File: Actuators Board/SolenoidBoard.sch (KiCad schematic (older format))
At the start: 33 parts, among them J10 Conn_01x02_Male, J9 Conn_01x02_Male, Q1 MMDT2222A

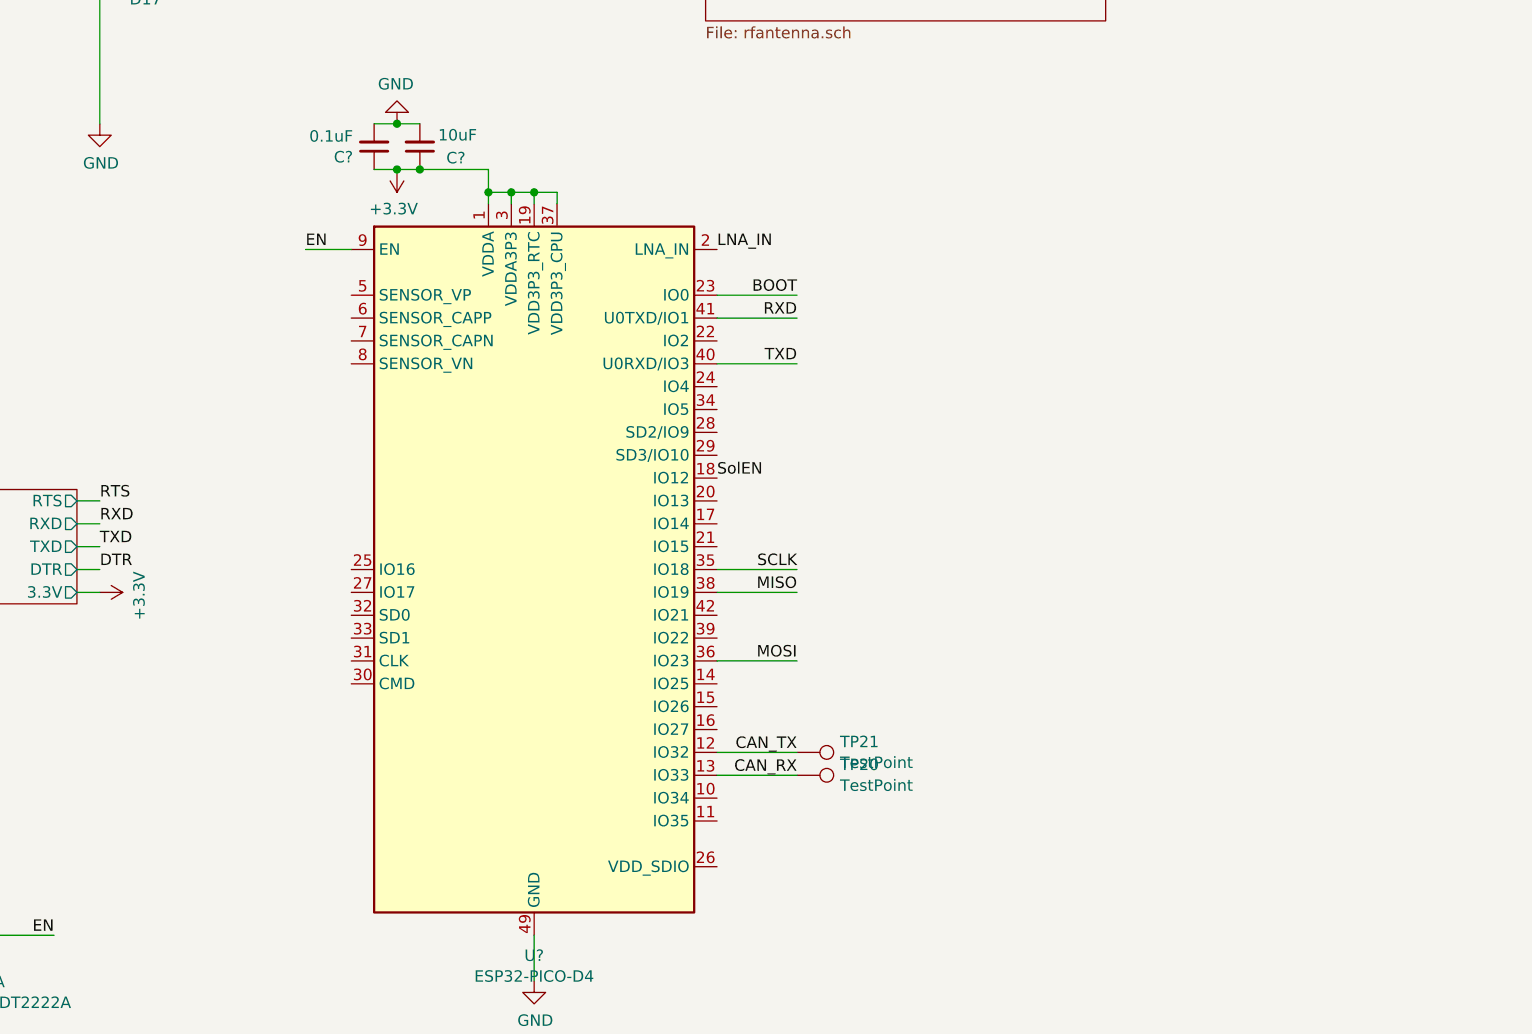
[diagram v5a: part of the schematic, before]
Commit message: added test points and power connectors (solenoid)
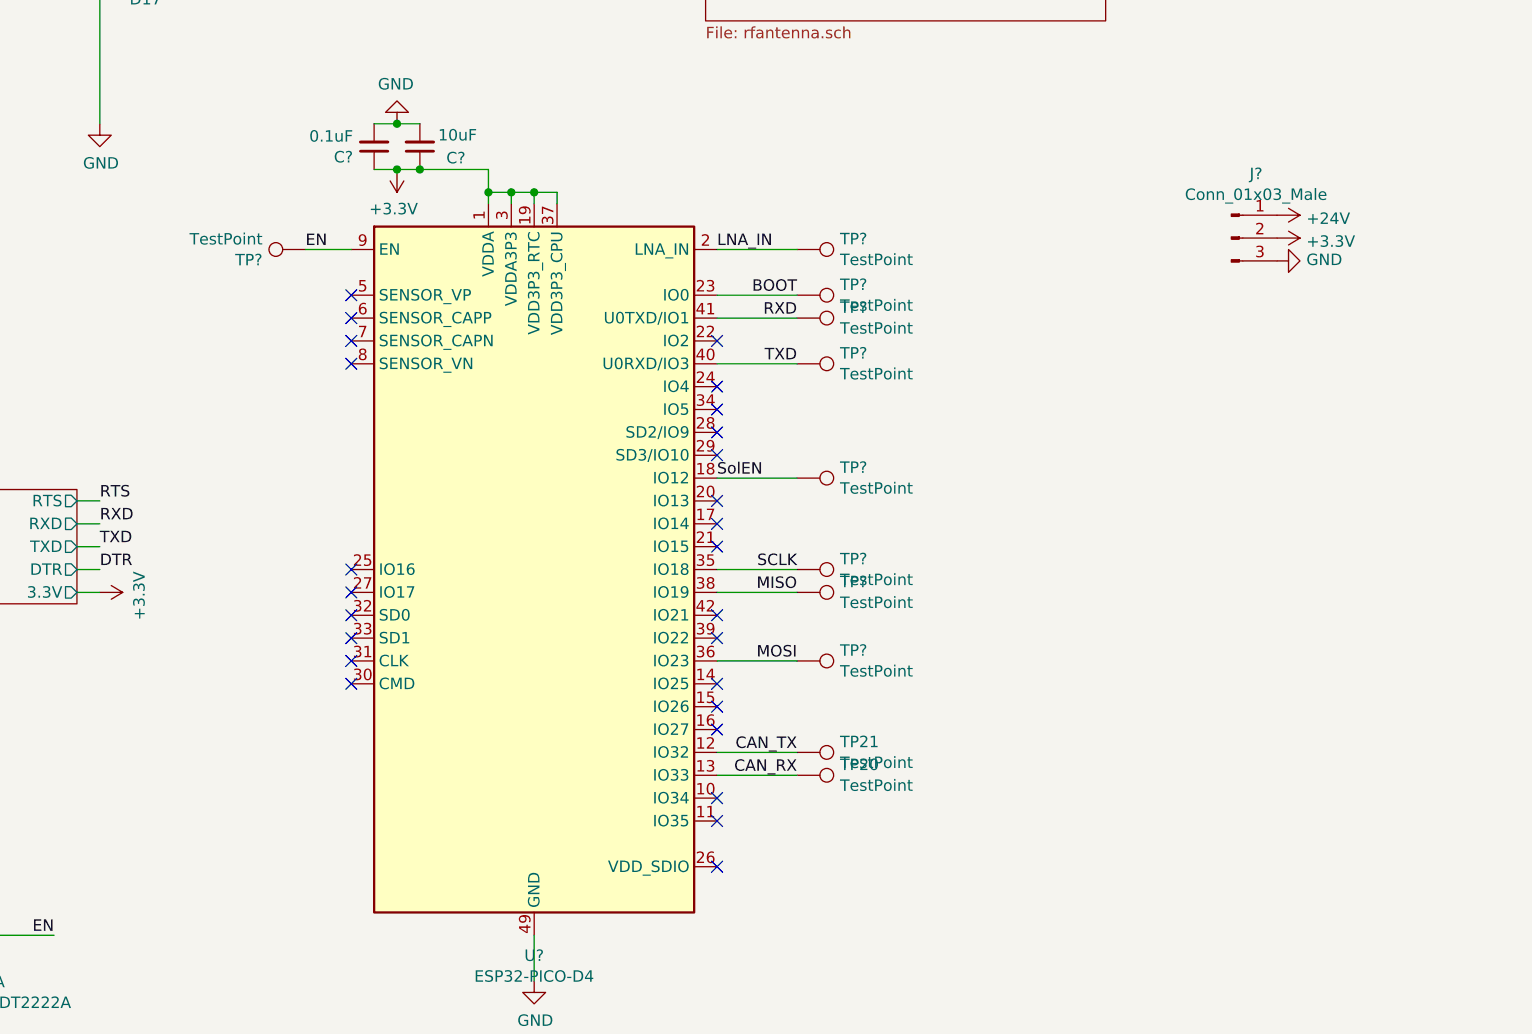
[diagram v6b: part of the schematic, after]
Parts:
- added J?: Conn_01x03_Male, symbol Connector:Conn_01x03_Male
- added TP? (x9): TestPoint, symbol Connector:TestPoint
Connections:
- net +24V: now also J?.1 (Pin_1)
- net +3V3: now also J?.2 (Pin_2)
- net BOOT: now also TP?.1
- net EN: now also TP?.1
- net GND: now also J?.3 (Pin_3)
- net LNA_IN: now also TP?.1
- net MISO: now also TP?.1
- net MOSI: now also TP?.1
- net RXD: now also TP?.1
- net SCLK: now also TP?.1
- net SolEN: now also TP?.1
- net TXD: now also TP?.1
- no-connect marks 0 -> 26
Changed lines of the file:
@@
 $EndComp
 Connection ~ 9800 2650
+$Comp
+L Connector:TestPoint TP?
+U 1 1 61AFDF58
+P 5350 2350
+F 0 "TP?" V 5304 2538 50  0000 L CNN
+F 1 "TestPoint" V 5395 2538 50  0000 L CNN
+F 2 "" H 5550 2350 50  0001 C CNN
+F 3 "~" H 5550 2350 50  0001 C CNN
+	1    5350 2350
+	0    1    1    0
+$EndComp
+$Comp
+L Connector:TestPoint TP?
+U 1 1 61AFF428
+P 5350 2450
+F 0 "TP?" V 5304 2638 50  0000 L CNN
+F 1 "TestPoint" V 5395 2638 50  0000 L CNN
+F 2 "" H 5550 2450 50  0001 C CNN
+F 3 "~" H 5550 2450 50  0001 C CNN
+	1    5350 2450
+	0    1    1    0
+$EndComp
+$Comp
+L Connector:TestPoint TP?
+U 1 1 61B026A5
+P 5350 2650
+F 0 "TP?" V 5304 2838 50  0000 L CNN
+F 1 "TestPoint" V 5395 2838 50  0000 L CNN
+F 2 "" H 5550 2650 50  0001 C CNN
+F 3 "~" H 5550 2650 50  0001 C CNN
+	1    5350 2650
+	0    1    1    0
+$EndComp
+$Comp
+L Connector:TestPoint TP?
+U 1 1 61B0576B
+P 5350 3550
+F 0 "TP?" V 5304 3738 50  0000 L CNN
+F 1 "TestPoint" V 5395 3738 50  0000 L CNN
+F 2 "" H 5550 3550 50  0001 C CNN
+F 3 "~" H 5550 3550 50  0001 C CNN
+	1    5350 3550
+	0    1    1    0
+$EndComp
+$Comp
+L Connector:TestPoint TP?
+U 1 1 61B088E5
+P 5350 3650
+F 0 "TP?" V 5304 3838 50  0000 L CNN
+F 1 "TestPoint" V 5395 3838 50  0000 L CNN
+F 2 "" H 5550 3650 50  0001 C CNN
+F 3 "~" H 5550 3650 50  0001 C CNN
+	1    5350 3650
+	0    1    1    0
+$EndComp
+$Comp
+L Connector:TestPoint TP?
+U 1 1 61B0B958
+P 5350 3950
+F 0 "TP?" V 5304 4138 50  0000 L CNN
+F 1 "TestPoint" V 5395 4138 50  0000 L CNN
+F 2 "" H 5550 3950 50  0001 C CNN
+F 3 "~" H 5550 3950 50  0001 C CNN
+	1    5350 3950
+	0    1    1    0
+$EndComp
+$Comp
+L Connector:TestPoint TP?
+U 1 1 61B0EC6F
+P 3200 2150
+F 0 "TP?" V 3154 2338 50  0000 L CNN
+F 1 "TestPoint" V 3245 2338 50  0000 L CNN
+F 2 "" H 3400 2150 50  0001 C CNN
+F 3 "~" H 3400 2150 50  0001 C CNN
+	1    3200 2150
+	0    -1   -1   0
+$EndComp
+$Comp
+L Connector:TestPoint TP?
+U 1 1 61B11C95
+P 5350 2150
+F 0 "TP?" V 5304 2338 50  0000 L CNN
+F 1 "TestPoint" V 5395 2338 50  0000 L CNN
+F 2 "" H 5550 2150 50  0001 C CNN
+F 3 "~" H 5550 2150 50  0001 C CNN
+	1    5350 2150
+	0    1    1    0
+$EndComp
+Wire Wire Line
+	5350 2150 5000 2150
+NoConn ~ 5000 3450
+NoConn ~ 5000 3350
+NoConn ~ 5000 3250
+NoConn ~ 5000 3050
+NoConn ~ 5000 2950
+NoConn ~ 5000 2850
+NoConn ~ 5000 2750
+$Comp
+L Connector:TestPoint TP?
+U 1 1 61B2ADC4
+P 5350 3150
+F 0 "TP?" V 5304 3338 50  0000 L CNN
+F 1 "TestPoint" V 5395 3338 50  0000 L CNN
+F 2 "" H 5550 3150 50  0001 C CNN
+F 3 "~" H 5550 3150 50  0001 C CNN
+	1    5350 3150
+	0    1    1    0
+$EndComp
+Wire Wire Line
+	5350 3150 5000 3150
+NoConn ~ 5000 3750
+NoConn ~ 5000 3850
+NoConn ~ 5000 4050
+NoConn ~ 5000 4150
+NoConn ~ 5000 4250
+NoConn ~ 5000 4550
+NoConn ~ 5000 4650
+NoConn ~ 5000 4850
+NoConn ~ 5000 2550
+NoConn ~ 3400 2350
+NoConn ~ 3400 2450
+NoConn ~ 3400 2550
+NoConn ~ 3400 2650
+NoConn ~ 3400 3550
+NoConn ~ 3400 3650
+NoConn ~ 3400 3750
+NoConn ~ 3400 3850
+NoConn ~ 3400 3950
+NoConn ~ 3400 4050
+$Comp
+L Connector:Conn_01x03_Male J?
+U 1 1 61B69127
+P 7250 2100
+F 0 "J?" H 7358 2381 50  0000 C CNN
+F 1 "Conn_01x03_Male" H 7358 2290 50  0000 C CNN
+F 2 "" H 7250 2100 50  0001 C CNN
+F 3 "~" H 7250 2100 50  0001 C CNN
+	1    7250 2100
+	1    0    0    -1
+$EndComp
+$Comp
+L power:+24V #PWR?
+U 1 1 61B6F94F
+P 7450 2000
+F 0 "#PWR?" H 7450 1850 50  0001 C CNN
+F 1 "+24V" V 7465 2128 50  0000 L CNN
+F 2 "" H 7450 2000 50  0001 C CNN
+F 3 "" H 7450 2000 50  0001 C CNN
+	1    7450 2000
+	0    1    1    0
+$EndComp
+$Comp
+L power:+3.3V #PWR?
+U 1 1 61B70540
+P 7450 2100
+F 0 "#PWR?" H 7450 1950 50  0001 C CNN
+F 1 "+3.3V" V 7465 2228 50  0000 L CNN
+F 2 "" H 7450 2100 50  0001 C CNN
+F 3 "" H 7450 2100 50  0001 C CNN
+	1    7450 2100
+	0    1    1    0
+$EndComp
+$Comp
+L power:GND #PWR?
+U 1 1 61B717A1
+P 7450 2200
+F 0 "#PWR?" H 7450 1950 50  0001 C CNN
+F 1 "GND" V 7455 2072 50  0000 R CNN
+F 2 "" H 7450 2200 50  0001 C CNN
+F 3 "" H 7450 2200 50  0001 C CNN
+	1    7450 2200
+	0    -1   -1   0
+$EndComp
 $EndSCHEMATC
